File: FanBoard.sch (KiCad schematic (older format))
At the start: 19 parts, among them J1 FAN1, J2 FAN2, J3 FAN3, J4 FAN4, J5 LDRBRDConn, Q1 BUK9M34-100EX, Q2 BUK9M34-100EX, Q3 BUK9M34-100EX, Q4 BUK9M34-100EX

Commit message: Updates reference
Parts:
- renumbered J5 to J1, J1 to J2, J2 to J3, J3 to J4, J4 to J5, LED to LED1
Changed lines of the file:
@@
 $EndComp
 $Comp
-L Connector_Generic:Conn_02x03_Top_Bottom J5
+L Connector_Generic:Conn_02x03_Top_Bottom J1
 U 1 1 5F1EEC57
 P 1300 4850
-F 0 "J5" H 1350 5167 50  0000 C CNN
+F 0 "J1" H 1350 5167 50  0000 C CNN
 F 1 "LDRBRDConn" H 1350 5076 50  0000 C CNN
 F 2 "Connector_Molex:Molex_Micro-Fit_3.0_43045-0612_2x03_P3.00mm_Vertical" H 1300 4850 50  0001 C CNN
@@
 $EndComp
 $Comp
-L Device:LED LED
+L Device:LED LED1
 U 1 1 5F1F72F0
 P 5250 5350
-F 0 "LED" V 5197 5430 50  0000 L CNN
+F 0 "LED1" V 5197 5430 50  0000 L CNN
 F 1 "STATUS" V 5288 5430 50  0000 L CNN
 F 2 "LED_SMD:LED_0805_2012Metric" H 5250 5350 50  0001 C CNN
@@
 $EndComp
 $Comp
-L Connector_Generic:Conn_01x02 J4
+L Connector_Generic:Conn_01x02 J5
 U 1 1 5F092946
 P 4250 5600
-F 0 "J4" H 4330 5592 50  0000 L CNN
+F 0 "J5" H 4330 5592 50  0000 L CNN
 F 1 "FAN4" H 4330 5501 50  0000 L CNN
 F 2 "UTSVT_Connectors:Molex_MicroFit3.0_1x2xP3.00mm_PolarizingPeg_Vertical" H 4250 5600 50  0001 C CNN
@@
 $EndComp
 $Comp
-L Connector_Generic:Conn_01x02 J3
+L Connector_Generic:Conn_01x02 J4
 U 1 1 5F092588
 P 4250 4950
-F 0 "J3" H 4330 4942 50  0000 L CNN
+F 0 "J4" H 4330 4942 50  0000 L CNN
 F 1 "FAN3" H 4330 4851 50  0000 L CNN
 F 2 "UTSVT_Connectors:Molex_MicroFit3.0_1x2xP3.00mm_PolarizingPeg_Vertical" H 4250 4950 50  0001 C CNN
@@
 $EndComp
 $Comp
-L Connector_Generic:Conn_01x02 J2
+L Connector_Generic:Conn_01x02 J3
 U 1 1 5F09203F
 P 4250 4300
-F 0 "J2" H 4330 4292 50  0000 L CNN
+F 0 "J3" H 4330 4292 50  0000 L CNN
 F 1 "FAN2" H 4330 4201 50  0000 L CNN
 F 2 "UTSVT_Connectors:Molex_MicroFit3.0_1x2xP3.00mm_PolarizingPeg_Vertical" H 4250 4300 50  0001 C CNN
@@
 $EndComp
 $Comp
-L Connector_Generic:Conn_01x02 J1
+L Connector_Generic:Conn_01x02 J2
 U 1 1 5F091D5D
 P 4250 3650
-F 0 "J1" H 4330 3642 50  0000 L CNN
+F 0 "J2" H 4330 3642 50  0000 L CNN
 F 1 "FAN1" H 4330 3551 50  0000 L CNN
 F 2 "UTSVT_Connectors:Molex_MicroFit3.0_1x2xP3.00mm_PolarizingPeg_Vertical" H 4250 3650 50  0001 C CNN

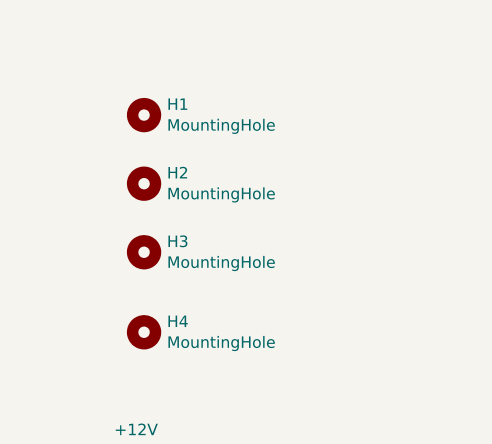
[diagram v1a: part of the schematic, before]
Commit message: Changed symbol and footprint library paths to include new repositories. Fixed issues with graphic footprints and reference labels
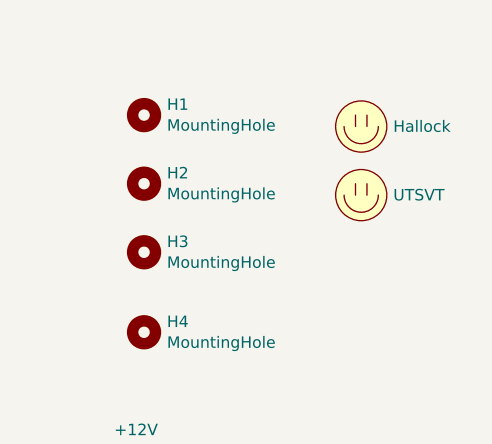
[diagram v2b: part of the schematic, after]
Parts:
- added LOGO1: Hallock, UTSVT_Special:Hallock_Image_Small, symbol utsvt-misc:Logo_Placeholder
- added LOGO2: UTSVT, UTSVT_Special:UTSVT_Logo_Symbol, symbol utsvt-misc:Logo_Placeholder
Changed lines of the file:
@@
+	1    0    0    -1
+$EndComp
+$Comp
+L utsvt-misc:Logo_Placeholder LOGO1
+U 1 1 5F29C39C
+P 6250 3700
+F 0 "LOGO1" H 6250 3850 50  0001 C CNN
+F 1 "Hallock" H 6390 3700 50  0000 L CNN
+F 2 "UTSVT_Special:Hallock_Image_Small" H 6250 3775 50  0001 C CNN
+F 3 "" H 6250 3775 50  0001 C CNN
+	1    6250 3700
+	1    0    0    -1
+$EndComp
+$Comp
+L utsvt-misc:Logo_Placeholder LOGO2
+U 1 1 5F29CCCF
+P 6250 4000
+F 0 "LOGO2" H 6250 4150 50  0001 C CNN
+F 1 "UTSVT" H 6390 4000 50  0000 L CNN
+F 2 "UTSVT_Special:UTSVT_Logo_Symbol" H 6250 4075 50  0001 C CNN
+F 3 "" H 6250 4075 50  0001 C CNN
+	1    6250 4000
 	1    0    0    -1
 $EndComp

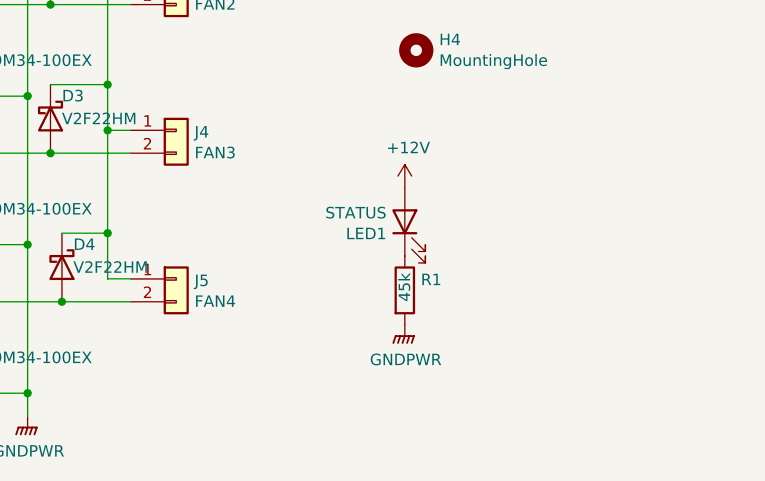
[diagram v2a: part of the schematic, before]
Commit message: Fixed resistor value and created Gerber files
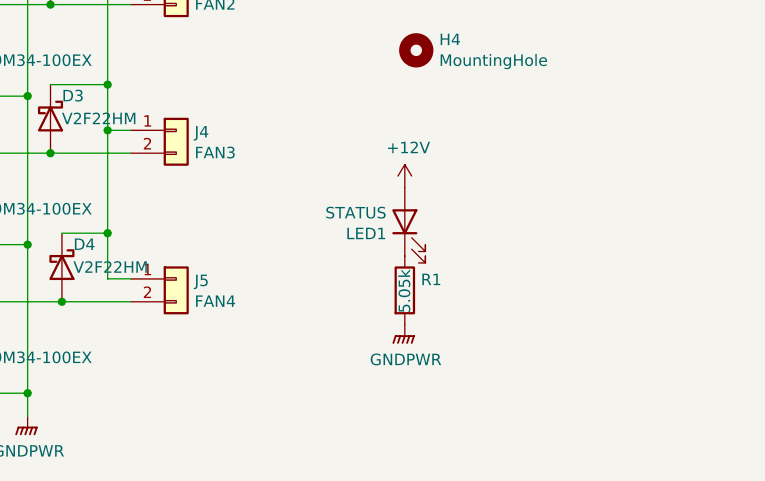
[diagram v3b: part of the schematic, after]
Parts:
- R1: value 45k -> 5.05k
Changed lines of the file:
@@
 P 5250 5650
 F 0 "R1" H 5320 5696 50  0000 L CNN
-F 1 "45k" V 5250 5600 50  0000 L CNN
+F 1 "5.05k" V 5250 5550 50  0000 L CNN
 F 2 "Resistor_SMD:R_0805_2012Metric" V 5180 5650 50  0001 C CNN
 F 3 "~" H 5250 5650 50  0001 C CNN
